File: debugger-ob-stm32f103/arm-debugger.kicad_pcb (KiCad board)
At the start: 2 copper layers, 44.2 x 16.6 mm, 27 parts, among them J1 USB_A, J2 Conn_02x05_Odd_Even, J3 Flash, J4 VDD, U1 STM32F103C8Tx, U2 6206, Y1 8M

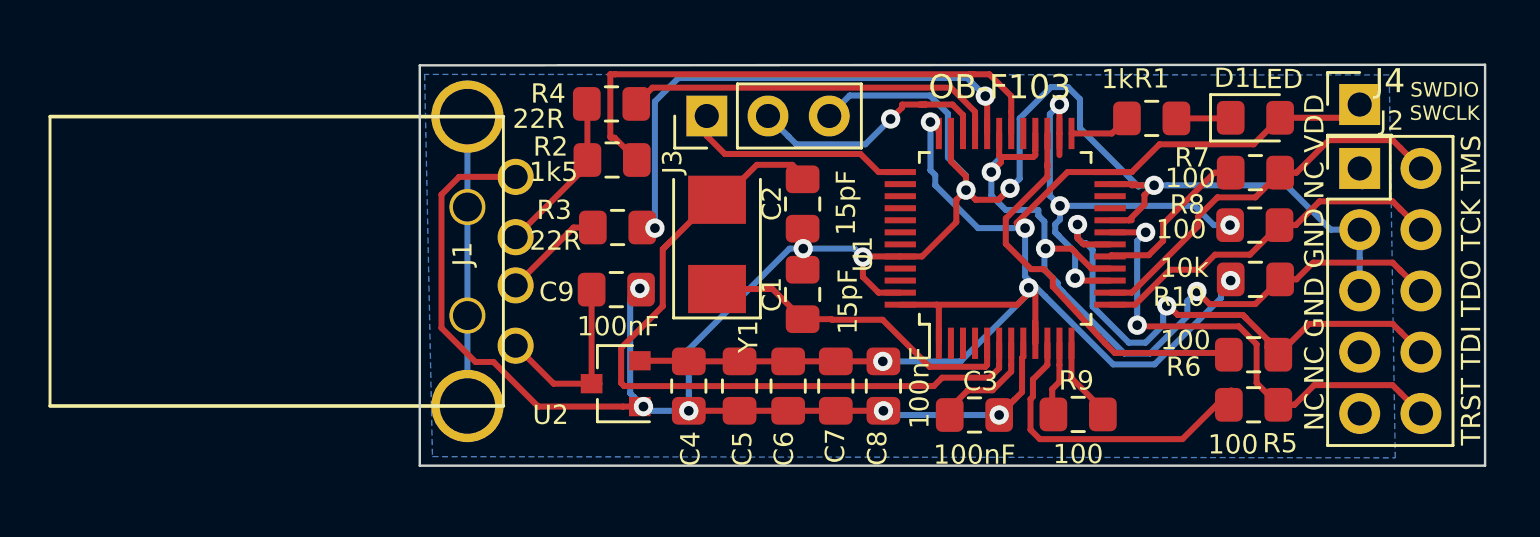
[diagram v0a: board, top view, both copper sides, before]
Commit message: Fix ob-stm32f103 for BOM
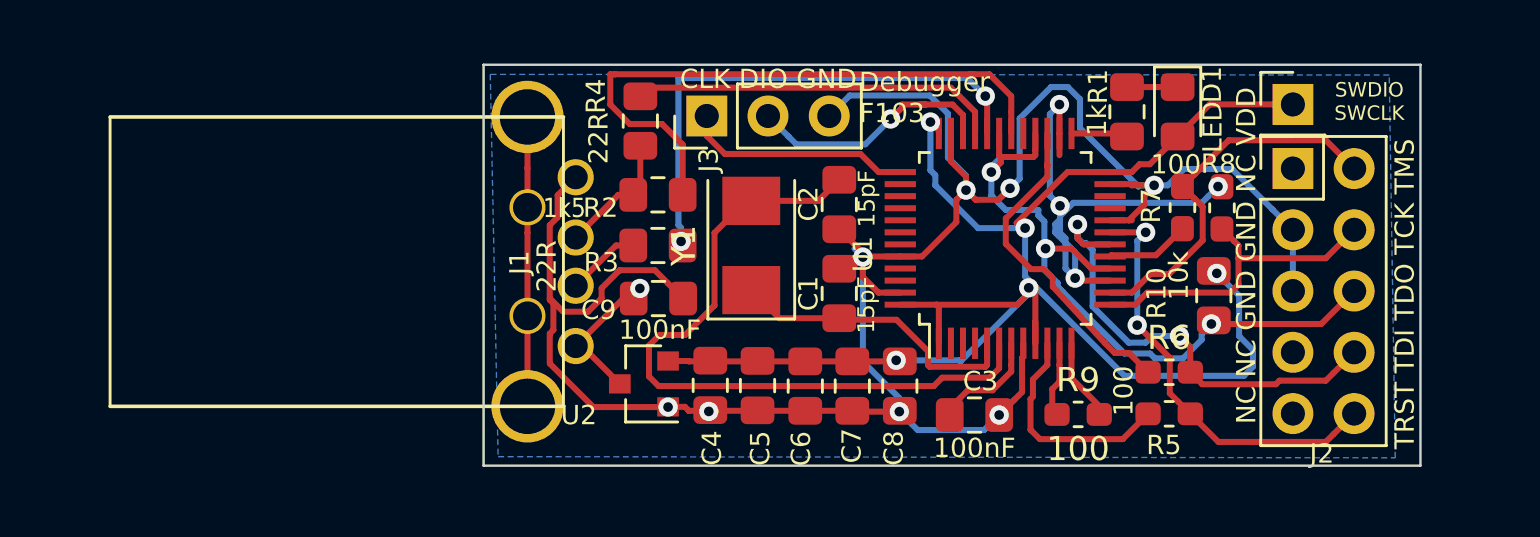
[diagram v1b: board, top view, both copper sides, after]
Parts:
- R5, R6, R7, R8, R9: footprint Resistor_SMD:R_0805_2012Metric_Pad1.15x1.40mm_HandSolder -> Resistor_SMD:R_0603_1608Metric_Pad1.05x0.95mm_HandSolder
- moved R6 3.57 mm to (100.7, 114.8)
- moved R5 3.52 mm to (100.7, 116.5)
- moved R7 3.35 mm to (101.2, 108.0), turned to 90 degrees
- moved D1 3.23 mm to (101.0, 104.0), turned to 270 degrees
- moved J2 2.77 mm to (105.8, 106.4)
- moved J4 2.77 mm to (105.8, 103.7)
- moved J1 2.49 mm to (76.1, 106.7)
- moved R2 2.39 mm to (79.5, 107.5)
- moved R10 1.85 mm to (102.5, 111.7), turned to 90 degrees
- moved R3 1.83 mm to (79.5, 109.6)
- moved C9 1.78 mm to (79.5, 111.8)
- moved R8 1.54 mm to (102.9, 108.0), turned to 270 degrees
- moved C1 1.52 mm to (87.0, 111.6)
- moved C2 1.52 mm to (87.0, 107.9)
- moved Y1 1.42 mm to (83.4, 109.6)
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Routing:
- net GND: track 109.0 -> 97.8 mm, vias 10 -> 8
- net Debugger-TDI-IN: track 23.6 -> 19.3 mm
- net Debugger-TDO-IN: track 34.4 -> 30.2 mm
- net Debugger-TRST-OUT: track 13.2 -> 9.35 mm
- net Debugger-TMS-OUT: track 6.85 -> 3.48 mm
- net Net-(R2-Pad2): track 22.8 -> 25.7 mm
- net Debugger-TDI-OUT: track 16.3 -> 13.8 mm
- net Debugger-TCK-OUT: track 19.2 -> 21.7 mm
- net Debugger-TRST-IN: track 20.4 -> 17.9 mm
- net 5V: track 8.16 -> 5.95 mm, vias 0 -> 1
- net USB-D+: track 6.93 -> 5.28 mm
- net Debugger-TCK-IN: track 15.2 -> 13.5 mm
- net Net-(C2-Pad1): track 31.1 -> 29.8 mm
- net USB-D-: track 4.19 -> 3.08 mm
- net Net-(C1-Pad1): track 13.5 -> 12.7 mm
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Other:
- board size 44.2 x 16.6 mm -> 38.9 x 16.6 mm
- board text added: "CLK DIO GND"
- board text added: "Debugger F103"
- board text removed: "OB-F103"
